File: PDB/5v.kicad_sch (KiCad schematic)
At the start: 30 parts, among them M1 GENERIC_MOSFET_N, M2 GENERIC_MOSFET_N, U8 LM5116MH/NOPB, U9 INA228

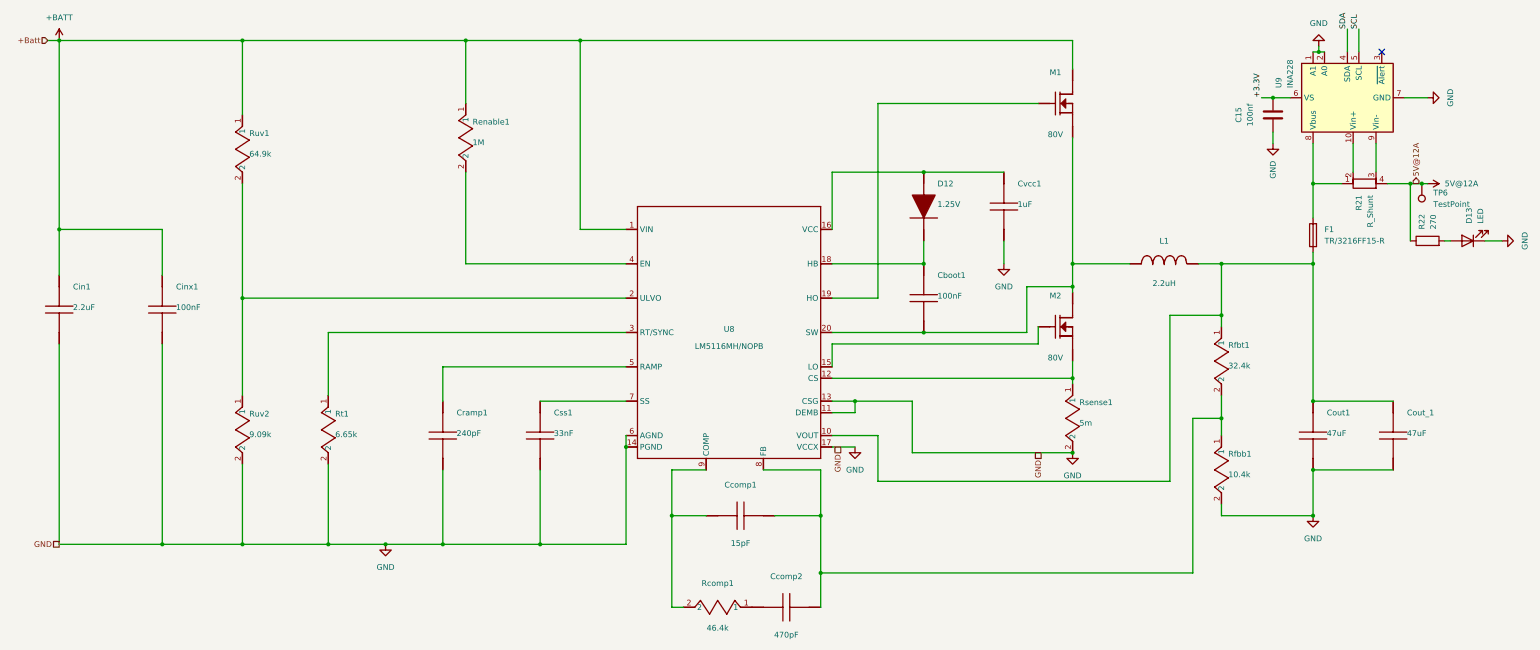
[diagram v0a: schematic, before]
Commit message: coordinated labels in schem
Labeled all components to be Rxx, Cxx, ext forms through all sheets so labels for BOM and layout are work together as one long list.
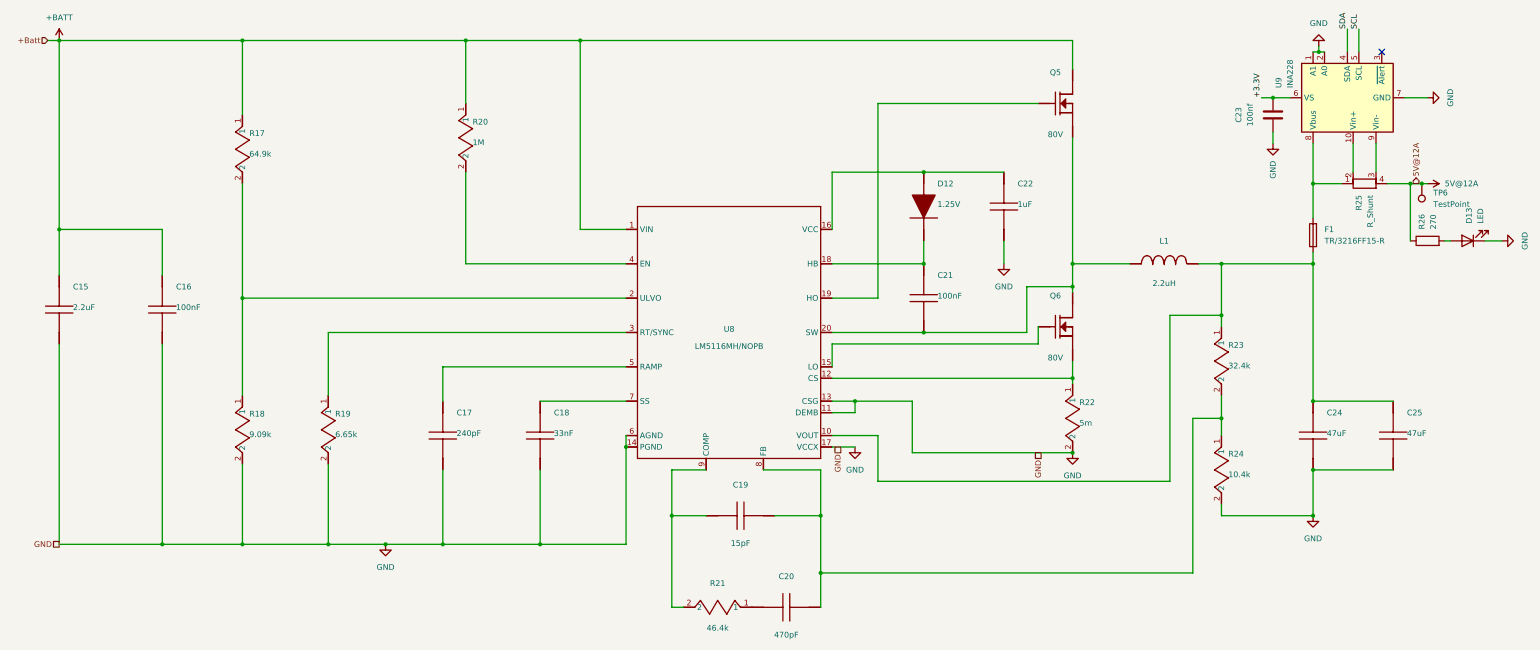
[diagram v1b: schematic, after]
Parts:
- renumbered Cin1 to C15, Cinx1 to C16, Cramp1 to C17, Css1 to C18, Ccomp1 to C19, Ccomp2 to C20, Cboot1 to C21, Cvcc1 to C22, C15 to C23, Cout1 to C24, Cout_1 to C25, M1 to Q5, M2 to Q6, Ruv1 to R17, Ruv2 to R18, Rt1 to R19, Renable1 to R20, Rcomp1 to R21, Rsense1 to R22, Rfbt1 to R23, Rfbb1 to R24, R21 to R25, R22 to R26

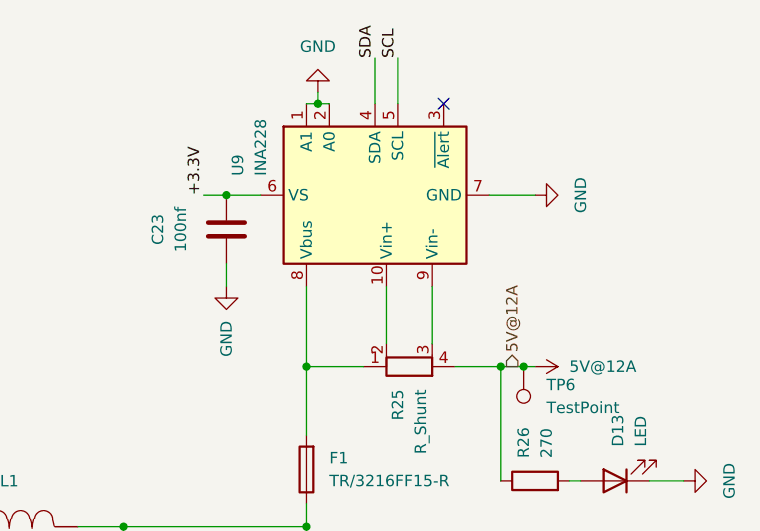
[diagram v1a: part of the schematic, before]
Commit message: last push before removing oring
i think we're going with an interlock system instead. the battery oring on here will take far too much physical room on the board to make it worthwhile. this push removes the oring and assumes a single power input.
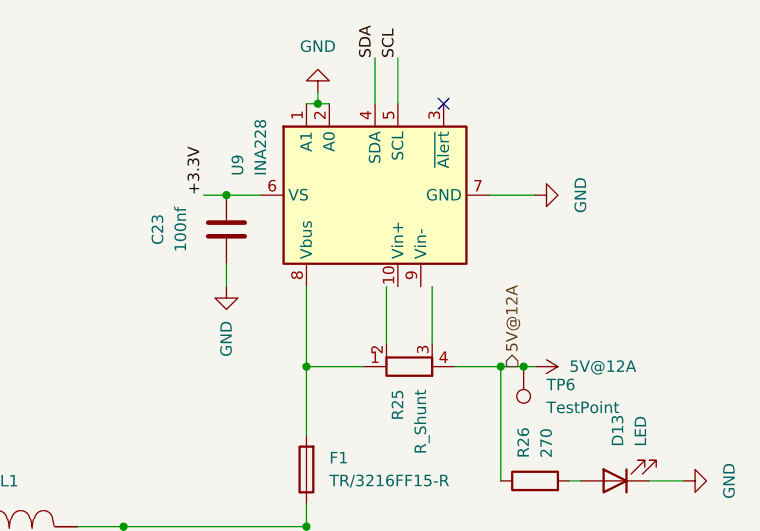
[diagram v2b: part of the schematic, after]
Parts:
- U9: footprint Package_SO:HVSSOP-10-1EP_3x3mm_P0.5mm_EP1.83x1.89mm -> Package_SO:TSSOP-10_3x3mm_P0.5mm
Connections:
- net at R25.2: no longer U9.10 (Vin+)
- net at R25.3: no longer U9.9 (Vin-)
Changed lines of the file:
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@@
 			)
 		)
-		(property "Footprint" "Package_SO:HVSSOP-10-1EP_3x3mm_P0.5mm_EP1.83x1.89mm"
+		(property "Footprint" "Package_SO:TSSOP-10_3x3mm_P0.5mm"
 			(at 413.004 79.248 0)
 			(hide yes)
